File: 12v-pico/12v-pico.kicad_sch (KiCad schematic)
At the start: 13 parts, among them J1 MERG 12v CBUS, J2 Adafruit CAN Pal, J3 Conn_01x03_Pin, J4 Conn_01x03_Pin, J5 Conn_01x20_Pin, J6 Conn_01x20_Pin, SW1 RESET, U1 LM7805_TO220

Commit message: tidied up schematic
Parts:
- J3: renamed from J4; value Conn_01x03_Pin -> DEBUG
- J4: renamed from J3; value Conn_01x03_Pin -> UART0
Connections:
- net GND: now also SW1.1; no longer SW1.2
- net at A1.30 (RUN), J6.11 (Pin_11): now also SW1.2; no longer SW1.1
- net +12V: no longer names the net of D1.2 (A), J1.1 (+12v)
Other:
- moved on the sheet: A1, C1, C2, D1, D2, J1, J2, J3, J4, J5, J6, SW1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

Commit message: design updates
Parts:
- J5: value Conn_01x20_Pin -> Pico LHS
- J6: value Conn_01x20_Pin -> Pico RHS
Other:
- title: 12v Pico -> 12v Pico + CAN
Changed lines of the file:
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@@
 	(paper "A4")
 	(title_block
-		(title "12v Pico")
+		(title "12v Pico + CAN")
 		(company "John McAleely")
+		(comment 1 "MERG CBUS Compatible Pico (12v, CAN tranciever)")
 	)
 	(junction
@@
 			)
 		)
-		(property "Value" "Conn_01x20_Pin"
+		(property "Value" "Pico LHS"
 			(at 34.798 136.906 0)
 			(effects
@@
 			)
 		)
-		(property "Value" "Conn_01x20_Pin"
+		(property "Value" "Pico RHS"
 			(at 176.022 136.652 0)
 			(effects
@@
 		)
 		(pin "1"
+			(alternate "VBUS")
 		)
 		(pin "2"

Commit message: update symbols and labels
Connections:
- net GND: now also J4.2 (GND); no longer J4.3 (Pin_3)
- net at A1.2 (GPIO1), J5.2 (Pin_2): now also J4.3 (RX); no longer J4.2 (Pin_2)
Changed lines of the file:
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@@
+	(wire
+		(pts
+			(xy 77.47 116.84) (xy 53.34 116.84)
+		)
+		(stroke
+			(width 0)
+			(type default)
+		)
+	)
 	(wire
 		(pts
@@
 	(wire
 		(pts
-			(xy 49.53 119.38) (xy 52.07 119.38)
-		)
-		(stroke
-			(width 0)
-			(type default)
-		)
-	)
-	(wire
-		(pts
 			(xy 80.01 152.4) (xy 59.69 152.4)
 		)
@@
 	(wire
 		(pts
+			(xy 49.53 119.38) (xy 53.34 119.38)
+		)
+		(stroke
+			(width 0)
+			(type default)
+		)
+	)
+	(wire
+		(pts
 			(xy 125.73 127) (xy 129.54 127)
 		)
@@
 	(wire
 		(pts
-			(xy 49.53 116.84) (xy 77.47 116.84)
-		)
-		(stroke
-			(width 0)
-			(type default)
-		)
-	)
-	(wire
-		(pts
 			(xy 76.2 119.38) (xy 76.2 143.51)
 		)
@@
 	(wire
 		(pts
-			(xy 52.07 119.38) (xy 52.07 120.65)
+			(xy 52.07 116.84) (xy 52.07 120.65)
 		)
 		(stroke
@@
 		(pts
 			(xy 78.74 114.3) (xy 80.01 114.3)
+		)
+		(stroke
+			(width 0)
+			(type default)
+		)
+	)
+	(wire
+		(pts
+			(xy 49.53 116.84) (xy 52.07 116.84)
+		)
+		(stroke
+			(width 0)
+			(type default)
+		)
+	)
+	(wire
+		(pts
+			(xy 53.34 116.84) (xy 53.34 119.38)
 		)
 		(stroke
@@
 		)
 		(property "Value" "UART0"
-			(at 39.116 118.11 0)
+			(at 36.322 119.634 0)
 			(effects
 				(font
@@
 	)
 	(symbol
+		(lib_name "Conn_01x03_Pin_1")
 		(lib_id "Connector:Conn_01x03_Pin")
 		(at 44.45 101.6 0)
@@
 		)
 		(property "Value" "DEBUG"
-			(at 38.354 103.124 0)
+			(at 34.036 102.616 0)
 			(effects
 				(font
@@
 		)
 		(pin "3"
+			(alternate "GND_IN")
 		)
 		(pin "38"
@@
 		)
 		(pin "2"
+			(alternate "UART0_RX")
 		)
 		(pin "37"
@@
 		)
 		(pin "1"
+			(alternate "UART0_TX")
 		)
 		(pin "D1"

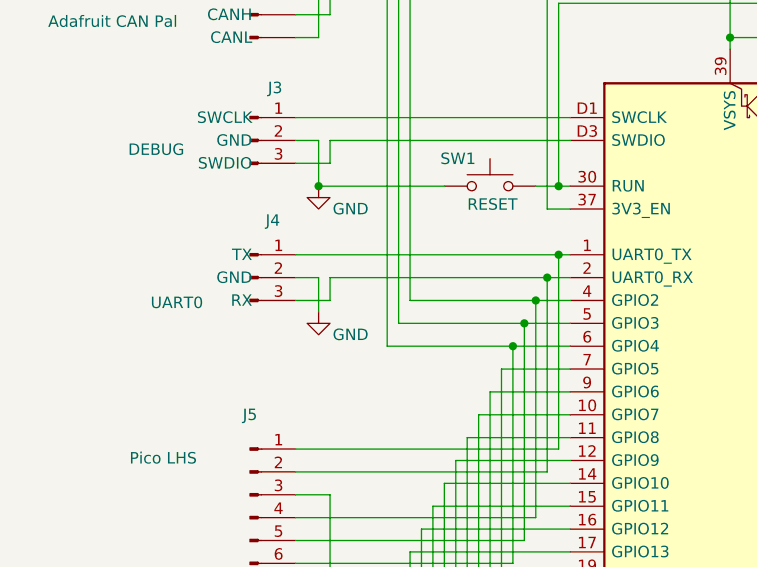
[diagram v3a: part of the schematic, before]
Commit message: even out board dimensions, label PCB
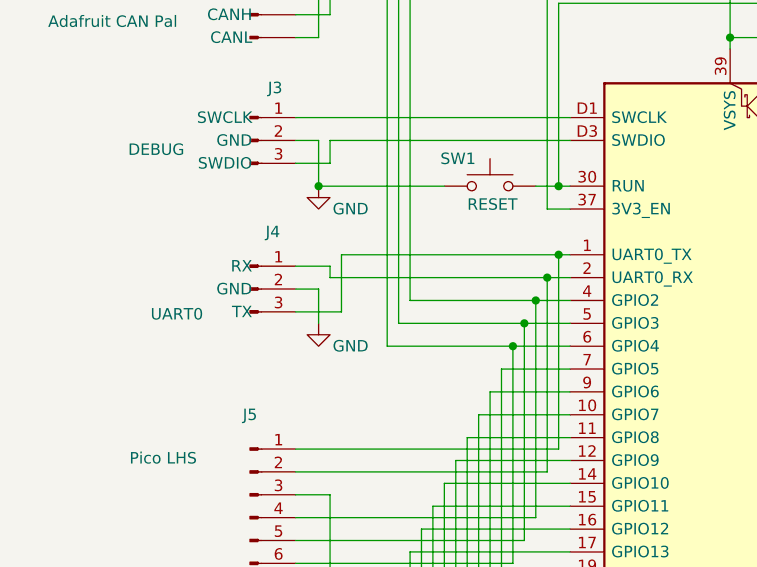
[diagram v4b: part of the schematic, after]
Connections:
- net at A1.1 (GPIO0), J5.1 (Pin_1): now also J4.3 (TX); no longer J4.1 (TX)
- net at A1.2 (GPIO1), J5.2 (Pin_2): now also J4.1 (RX); no longer J4.3 (RX)
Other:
- moved on the sheet: J4
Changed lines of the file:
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@@
+	)
+	(junction
+		(at 78.74 114.3)
+		(diameter 0)
+		(color 0 0 0 0)
 	)
 	(junction
@@
 	)
 	(junction
-		(at 78.74 114.3)
-		(diameter 0)
-		(color 0 0 0 0)
-	)
-	(junction
 		(at 97.79 90.17)
 		(diameter 0)
@@
 	)
 	(junction
-		(at 77.47 116.84)
-		(diameter 0)
-		(color 0 0 0 0)
-	)
-	(junction
 		(at 71.12 36.83)
 		(diameter 0)
@@
 	)
 	(junction
+		(at 77.47 116.84)
+		(diameter 0)
+		(color 0 0 0 0)
+	)
+	(junction
 		(at 147.32 166.37)
 		(diameter 0)
@@
 	(wire
 		(pts
-			(xy 49.53 114.3) (xy 78.74 114.3)
-		)
-		(stroke
-			(width 0)
-			(type default)
-		)
-	)
-	(wire
-		(pts
 			(xy 125.73 137.16) (xy 143.51 137.16)
 		)
@@
 	(wire
 		(pts
+			(xy 54.61 114.3) (xy 78.74 114.3)
+		)
+		(stroke
+			(width 0)
+			(type default)
+		)
+	)
+	(wire
+		(pts
 			(xy 80.01 124.46) (xy 73.66 124.46)
 		)
@@
 	(wire
 		(pts
+			(xy 53.34 116.84) (xy 77.47 116.84)
+		)
+		(stroke
+			(width 0)
+			(type default)
+		)
+	)
+	(wire
+		(pts
 			(xy 125.73 142.24) (xy 138.43 142.24)
 		)
@@
 	(wire
 		(pts
-			(xy 77.47 116.84) (xy 53.34 116.84)
-		)
-		(stroke
-			(width 0)
-			(type default)
-		)
-	)
-	(wire
-		(pts
 			(xy 64.77 171.45) (xy 49.53 171.45)
 		)
@@
 	(wire
 		(pts
+			(xy 53.34 115.57) (xy 53.34 116.84)
+		)
+		(stroke
+			(width 0)
+			(type default)
+		)
+	)
+	(wire
+		(pts
 			(xy 53.34 187.96) (xy 83.82 187.96)
 		)
@@
 	(wire
 		(pts
-			(xy 49.53 119.38) (xy 53.34 119.38)
+			(xy 49.53 120.65) (xy 54.61 120.65)
 		)
 		(stroke
@@
 	(wire
 		(pts
-			(xy 52.07 116.84) (xy 52.07 120.65)
+			(xy 52.07 118.11) (xy 52.07 121.92)
 		)
 		(stroke
@@
 	(wire
 		(pts
-			(xy 49.53 116.84) (xy 52.07 116.84)
-		)
-		(stroke
-			(width 0)
-			(type default)
-		)
-	)
-	(wire
-		(pts
-			(xy 53.34 116.84) (xy 53.34 119.38)
+			(xy 49.53 118.11) (xy 52.07 118.11)
 		)
 		(stroke
@@
 	(wire
 		(pts
+			(xy 49.53 115.57) (xy 53.34 115.57)
+		)
+		(stroke
+			(width 0)
+			(type default)
+		)
+	)
+	(wire
+		(pts
 			(xy 49.53 63.5) (xy 53.34 63.5)
 		)
@@
 		(pts
 			(xy 80.01 142.24) (xy 64.77 142.24)
+		)
+		(stroke
+			(width 0)
+			(type default)
+		)
+	)
+	(wire
+		(pts
+			(xy 54.61 120.65) (xy 54.61 114.3)
 		)
 		(stroke
@@
 	(symbol
 		(lib_id "Connector:Conn_01x03_Pin")
-		(at 44.45 116.84 0)
+		(at 44.45 118.11 0)
 		(unit 1)
 		(exclude_from_sim no)
@@
 		(dnp no)
 		(property "Reference" "J4"
-			(at 46.99 110.49 0)
+			(at 46.99 111.76 0)
 			(effects
 				(font
@@
 		)
 		(property "Value" "UART0"
-			(at 36.322 119.634 0)
+			(at 36.322 120.904 0)
 			(effects
 				(font
@@
 		)
 		(property "Footprint" "Connector_PinSocket_2.54mm:PinSocket_1x03_P2.54mm_Vertical"
-			(at 44.45 116.84 0)
+			(at 44.45 118.11 0)
 			(effects
 				(font
@@
 		)
 		(property "Datasheet" "~"
-			(at 44.45 116.84 0)
+			(at 44.45 118.11 0)
 			(effects
 				(font
@@
 		)
 		(property "Description" "Generic connector, single row, 01x03, script generated"
-			(at 44.45 116.84 0)
+			(at 44.45 118.11 0)
 			(effects
 				(font
@@
 	(symbol
 		(lib_id "power:GND")
-		(at 52.07 120.65 0)
+		(at 52.07 121.92 0)
 		(unit 1)
 		(exclude_from_sim no)
@@
 		(dnp no)
 		(property "Reference" "#PWR03"
-			(at 52.07 127 0)
+			(at 52.07 128.27 0)
 			(effects
 				(font
@@
 		)
 		(property "Value" "GND"
-			(at 55.626 123.19 0)
+			(at 55.626 124.46 0)
 			(effects
 				(font
@@
 		)
 		(property "Footprint" ""
-			(at 52.07 120.65 0)
+			(at 52.07 121.92 0)
 			(effects
 				(font
@@
 		)
 		(property "Datasheet" ""
-			(at 52.07 120.65 0)
+			(at 52.07 121.92 0)
 			(effects
 				(font
@@
 		)
 		(property "Description" "Power symbol creates a global label with name \"GND\" , ground"
-			(at 52.07 120.65 0)
-			(effects
-				(font
+			(at 52.07 121.92 0)
+			(effects
+				(font
